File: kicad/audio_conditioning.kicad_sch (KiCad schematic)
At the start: 51 parts, among them Q5 MMUN2111LT1G, Q6 MMUN2111LT1G, Q7 MMBT3904, Q8 MMBT3904, U4 OPA1678, U5 OPA1678, U6 OPA1678

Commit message: started with PCB layout. Might want to move I2S
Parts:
- C24: renamed from C42; footprint (none) -> Capacitor_SMD:C_0805_2012Metric
- C25: renamed from C43; footprint (none) -> Capacitor_SMD:C_0805_2012Metric
- C26: renamed from C45; footprint (none) -> Capacitor_SMD:C_0402_1005Metric
- C27: renamed from C44; footprint (none) -> Capacitor_SMD:C_0402_1005Metric
- C28: renamed from C52; footprint (none) -> Capacitor_SMD:C_0603_1608Metric
- C29: renamed from C53; footprint (none) -> Capacitor_SMD:C_0603_1608Metric
- C30: renamed from C54; footprint (none) -> Capacitor_SMD:C_0603_1608Metric
- C31: renamed from C55; footprint (none) -> Capacitor_SMD:C_0603_1608Metric
- C32: renamed from C60; footprint (none) -> Capacitor_SMD:C_0402_1005Metric
- C33: renamed from C62; footprint (none) -> Capacitor_SMD:C_0603_1608Metric
- C34: renamed from C64; footprint (none) -> Capacitor_SMD:CP_Elec_4x5.4
- C35: renamed from C58; footprint (none) -> Capacitor_SMD:CP_Elec_4x5.4
- C36: renamed from C56; footprint (none) -> Capacitor_SMD:C_0603_1608Metric
- C37: renamed from C57; footprint (none) -> Capacitor_SMD:C_0603_1608Metric
- C38: renamed from C61; footprint (none) -> Capacitor_SMD:C_0402_1005Metric
- C39: renamed from C63; footprint (none) -> Capacitor_SMD:C_0603_1608Metric
- C40: renamed from C65; footprint (none) -> Capacitor_SMD:CP_Elec_4x5.4
- C41: renamed from C59; footprint (none) -> Capacitor_SMD:CP_Elec_4x5.4
- R20: renamed from R36; footprint (none) -> Resistor_SMD:R_0402_1005Metric
- R21: renamed from R37; footprint (none) -> Resistor_SMD:R_0402_1005Metric
- R22: renamed from R39; footprint (none) -> Resistor_SMD:R_0402_1005Metric
- R23: renamed from R40; footprint (none) -> Resistor_SMD:R_0402_1005Metric
- R24: renamed from R38; footprint (none) -> Resistor_SMD:R_0402_1005Metric
- R25: renamed from R41; footprint (none) -> Resistor_SMD:R_0402_1005Metric
- R26: renamed from R51; footprint (none) -> Resistor_SMD:R_0402_1005Metric
- R27: renamed from R57; footprint (none) -> Resistor_SMD:R_0402_1005Metric
- R28: renamed from R52; footprint (none) -> Resistor_SMD:R_0402_1005Metric
- R29: renamed from R58; footprint (none) -> Resistor_SMD:R_0402_1005Metric
- R30: renamed from R61; footprint (none) -> Resistor_SMD:R_0402_1005Metric
- R31: renamed from R55; footprint (none) -> Resistor_SMD:R_0402_1005Metric
- R32: renamed from R63; footprint (none) -> Resistor_SMD:R_0402_1005Metric
- R33: renamed from R65; footprint (none) -> Resistor_SMD:R_0402_1005Metric
- R34: renamed from R69; footprint (none) -> Resistor_SMD:R_0402_1005Metric
- R35: renamed from R67; footprint (none) -> Resistor_SMD:R_0402_1005Metric
- R36: renamed from R53; footprint (none) -> Resistor_SMD:R_0402_1005Metric
- R37: renamed from R59; footprint (none) -> Resistor_SMD:R_0402_1005Metric
- R38: renamed from R54; footprint (none) -> Resistor_SMD:R_0402_1005Metric
- R39: renamed from R60; footprint (none) -> Resistor_SMD:R_0402_1005Metric
- R40: renamed from R62; footprint (none) -> Resistor_SMD:R_0402_1005Metric
- R41: renamed from R56; footprint (none) -> Resistor_SMD:R_0402_1005Metric
- R42: renamed from R64; footprint (none) -> Resistor_SMD:R_0402_1005Metric
- R43: renamed from R66; footprint (none) -> Resistor_SMD:R_0402_1005Metric
- R44: renamed from R70; footprint (none) -> Resistor_SMD:R_0402_1005Metric
- R45: renamed from R68; footprint (none) -> Resistor_SMD:R_0402_1005Metric
- U4, U5, U6: footprint (none) -> Package_SO:SOIC-8_3.9x4.9mm_P1.27mm

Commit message: aaaa
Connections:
- net at C38.2, R37.2: now also U6.2 (-); no longer U6.6 (-)
- net at C40.1: now also U6.1; no longer U6.7
- net at C33.2, R29.2: now also U6.5 (+); no longer U6.3 (+)
- net at C32.2, R27.2: now also U6.6 (-); no longer U6.2 (-)
- net at C34.1: now also U6.7; no longer U6.1
- net at C39.2, R39.2: now also U6.3 (+); no longer U6.5 (+)
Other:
- moved on the sheet: U4C, U5C, U6C
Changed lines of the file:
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@@
 	)
 	(junction
-		(at 49.53 152.4)
+		(at 62.23 125.73)
 		(diameter 0)
 		(color 0 0 0 0)
@@
 	)
 	(junction
-		(at 45.72 176.53)
+		(at 58.42 149.86)
 		(diameter 0)
 		(color 0 0 0 0)
 	)
 	(junction
-		(at 45.72 152.4)
+		(at 58.42 125.73)
 		(diameter 0)
 		(color 0 0 0 0)
@@
 	)
 	(junction
-		(at 40.64 176.53)
+		(at 53.34 149.86)
 		(diameter 0)
 		(color 0 0 0 0)
@@
 	(wire
 		(pts
-			(xy 45.72 152.4) (xy 45.72 157.48)
+			(xy 58.42 125.73) (xy 58.42 130.81)
 		)
 		(stroke
@@
 	(wire
 		(pts
-			(xy 30.48 172.72) (xy 30.48 176.53)
+			(xy 43.18 146.05) (xy 43.18 149.86)
 		)
 		(stroke
@@
 	(wire
 		(pts
-			(xy 45.72 172.72) (xy 45.72 176.53)
+			(xy 58.42 146.05) (xy 58.42 149.86)
 		)
 		(stroke
@@
 	(wire
 		(pts
-			(xy 62.23 157.48) (xy 62.23 152.4)
+			(xy 74.93 130.81) (xy 74.93 125.73)
 		)
 		(stroke
@@
 	(wire
 		(pts
-			(xy 30.48 157.48) (xy 30.48 152.4)
+			(xy 43.18 130.81) (xy 43.18 125.73)
 		)
 		(stroke
@@
 	(wire
 		(pts
-			(xy 30.48 176.53) (xy 40.64 176.53)
+			(xy 43.18 149.86) (xy 53.34 149.86)
 		)
 		(stroke
@@
 	(wire
 		(pts
-			(xy 62.23 172.72) (xy 62.23 176.53)
+			(xy 74.93 146.05) (xy 74.93 149.86)
 		)
 		(stroke
@@
 	(wire
 		(pts
-			(xy 49.53 152.4) (xy 45.72 152.4)
+			(xy 62.23 125.73) (xy 58.42 125.73)
 		)
 		(stroke
@@
 	(wire
 		(pts
-			(xy 40.64 176.53) (xy 45.72 176.53)
+			(xy 53.34 149.86) (xy 58.42 149.86)
 		)
 		(stroke
@@
 	(wire
 		(pts
-			(xy 40.64 176.53) (xy 40.64 179.07)
+			(xy 53.34 149.86) (xy 53.34 152.4)
 		)
 		(stroke
@@
 	(wire
 		(pts
-			(xy 62.23 152.4) (xy 49.53 152.4)
+			(xy 74.93 125.73) (xy 62.23 125.73)
 		)
 		(stroke
@@
 	(wire
 		(pts
-			(xy 30.48 152.4) (xy 45.72 152.4)
+			(xy 43.18 125.73) (xy 58.42 125.73)
 		)
 		(stroke
@@
 	(wire
 		(pts
-			(xy 62.23 176.53) (xy 45.72 176.53)
+			(xy 74.93 149.86) (xy 58.42 149.86)
 		)
 		(stroke
@@
 	(symbol
 		(lib_id "Amplifier_Operational:OPA1678")
-		(at 33.02 165.1 0)
+		(at 45.72 138.43 0)
 		(unit 3)
 		(body_style 1)
@@
 		(dnp no)
 		(property "Reference" "U4"
-			(at 32.512 167.386 0)
+			(at 45.212 140.716 0)
 			(show_name no)
 			(do_not_autoplace no)
@@
 		)
 		(property "Value" "OPA1678"
-			(at 32.258 164.592 0)
+			(at 44.958 137.922 0)
 			(show_name no)
 			(do_not_autoplace no)
@@
 		)
 		(property "Footprint" "Package_SO:SOIC-8_3.9x4.9mm_P1.27mm"
-			(at 33.02 165.1 0)
+			(at 45.72 138.43 0)
 			(hide yes)
 			(show_name no)
@@
 		)
 		(property "Datasheet" "http://www.ti.com/lit/ds/symlink/opa1678.pdf"
-			(at 33.02 165.1 0)
+			(at 45.72 138.43 0)
 			(hide yes)
 			(show_name no)
@@
 		)
 		(property "Description" "Low-Distortion Audio Operational Amplifiers, SOIC-8/VSSOP-8"
-			(at 33.02 165.1 0)
+			(at 45.72 138.43 0)
 			(hide yes)
 			(show_name no)
@@
 		(at 182.88 107.95 0)
 		(mirror x)
-		(unit 2)
+		(unit 1)
 		(body_style 1)
 		(exclude_from_sim no)
@@
 				(path "/820f84be-8ed9-43fe-8cf8-9ca6f73c98d0"
 					(reference "U6")
-					(unit 2)
+					(unit 1)
 				)
 			)
@@
 	(symbol
 		(lib_id "Amplifier_Operational:OPA1678")
-		(at 43.18 165.1 0)
+		(at 55.88 138.43 0)
 		(mirror y)
 		(unit 3)
@@
 		(dnp no)
 		(property "Reference" "U5"
-			(at 46.99 166.3701 0)
+			(at 59.69 139.7001 0)
 			(show_name no)
 			(do_not_autoplace no)
@@
 		)
 		(property "Value" "OPA1678"
-			(at 46.99 163.8301 0)
+			(at 59.69 137.1601 0)
 			(show_name no)
 			(do_not_autoplace no)
@@
 		)
 		(property "Footprint" "Package_SO:SOIC-8_3.9x4.9mm_P1.27mm"
-			(at 43.18 165.1 0)
+			(at 55.88 138.43 0)
 			(hide yes)
 			(show_name no)
@@
 		)
 		(property "Datasheet" "http://www.ti.com/lit/ds/symlink/opa1678.pdf"
-			(at 43.18 165.1 0)
+			(at 55.88 138.43 0)
 			(hide yes)
 			(show_name no)
@@
 		)
 		(property "Description" "Low-Distortion Audio Operational Amplifiers, SOIC-8/VSSOP-8"
-			(at 43.18 165.1 0)
+			(at 55.88 138.43 0)
 			(hide yes)
 			(show_name no)
@@
 		(at 182.88 44.45 0)
 		(mirror x)
-		(unit 1)
+		(unit 2)
 		(body_style 1)
 		(exclude_from_sim no)
@@
 				(path "/820f84be-8ed9-43fe-8cf8-9ca6f73c98d0"
 					(reference "U6")
-					(unit 1)
+					(unit 2)
 				)
 			)
@@
 	(symbol
 		(lib_id "power:GND")
-		(at 40.64 179.07 0)
+		(at 53.34 152.4 0)
 		(unit 1)
 		(body_style 1)
@@
 		(fields_autoplaced yes)
 		(property "Reference" "#PWR052"
-			(at 40.64 185.42 0)
+			(at 53.34 158.75 0)
 			(hide yes)
 			(show_name no)
@@
 		)
 		(property "Value" "GND"
-			(at 40.64 184.15 0)
+			(at 53.34 157.48 0)
 			(hide yes)
 			(show_name no)
@@
 		)
 		(property "Footprint" ""
-			(at 40.64 179.07 0)
+			(at 53.34 152.4 0)
 			(hide yes)
 			(show_name no)
@@
 		)
 		(property "Datasheet" ""
-			(at 40.64 179.07 0)
+			(at 53.34 152.4 0)
 			(hide yes)
 			(show_name no)
@@
 		)
 		(property "Description" "Power symbol creates a global label with name \"GND\" , ground"
-			(at 40.64 179.07 0)
+			(at 53.34 152.4 0)
 			(hide yes)
 			(show_name no)
@@
 	(symbol
 		(lib_id "Amplifier_Operational:OPA1678")
-		(at 59.69 165.1 0)
+		(at 72.39 138.43 0)
 		(mirror y)
 		(unit 3)
@@
 		(dnp no)
 		(property "Reference" "U6"
-			(at 64.77 166.116 0)
+			(at 77.47 139.446 0)
 			(show_name no)
 			(do_not_autoplace no)
@@
 		)
 		(property "Value" "OPA1678"
-			(at 64.77 163.83 0)
+			(at 77.47 137.16 0)
 			(show_name no)
 			(do_not_autoplace no)
@@
 		)
 		(property "Footprint" "Package_SO:SOIC-8_3.9x4.9mm_P1.27mm"
-			(at 59.69 165.1 0)
+			(at 72.39 138.43 0)
 			(hide yes)
 			(show_name no)
@@
 		)
 		(property "Datasheet" "http://www.ti.com/lit/ds/symlink/opa1678.pdf"
-			(at 59.69 165.1 0)
+			(at 72.39 138.43 0)
 			(hide yes)
 			(show_name no)
@@
 		)
 		(property "Description" "Low-Distortion Audio Operational Amplifiers, SOIC-8/VSSOP-8"
-			(at 59.69 165.1 0)
+			(at 72.39 138.43 0)
 			(hide yes)
 			(show_name no)
@@
 	(symbol
 		(lib_id "power:+5VA")
-		(at 49.53 152.4 0)
+		(at 62.23 125.73 0)
 		(unit 1)
 		(body_style 1)
@@
 		(fields_autoplaced yes)
 		(property "Reference" "#PWR053"
-			(at 49.53 156.21 0)
+			(at 62.23 129.54 0)
 			(hide yes)
 			(show_name no)
@@
 		)
 		(property "Value" "+5VA"
-			(at 49.53 147.32 0)
+			(at 62.23 120.65 0)
 			(show_name no)
 			(do_not_autoplace no)
@@
 		)
 		(property "Footprint" ""
-			(at 49.53 152.4 0)
+			(at 62.23 125.73 0)
 			(hide yes)
 			(show_name no)
@@
 		)
 		(property "Datasheet" ""
-			(at 49.53 152.4 0)
+			(at 62.23 125.73 0)
 			(hide yes)
 			(show_name no)
@@
 		)
 		(property "Description" "Power symbol creates a global label with name \"+5VA\""
-			(at 49.53 152.4 0)
+			(at 62.23 125.73 0)
 			(hide yes)
 			(show_name no)

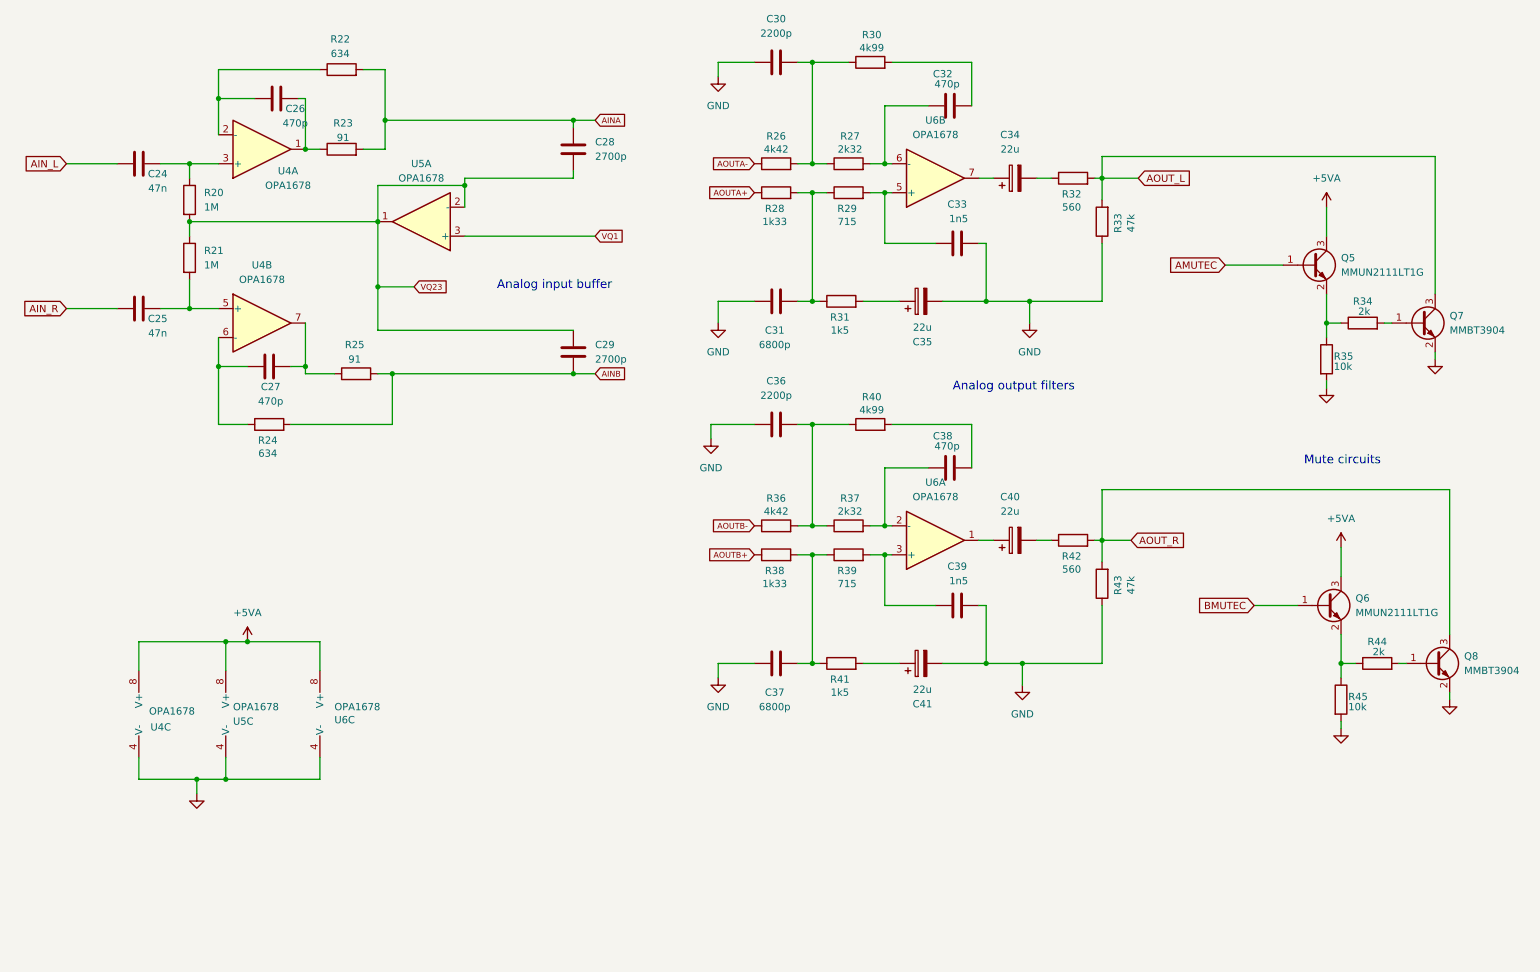
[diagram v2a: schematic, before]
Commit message: moved to hierarchical sheets
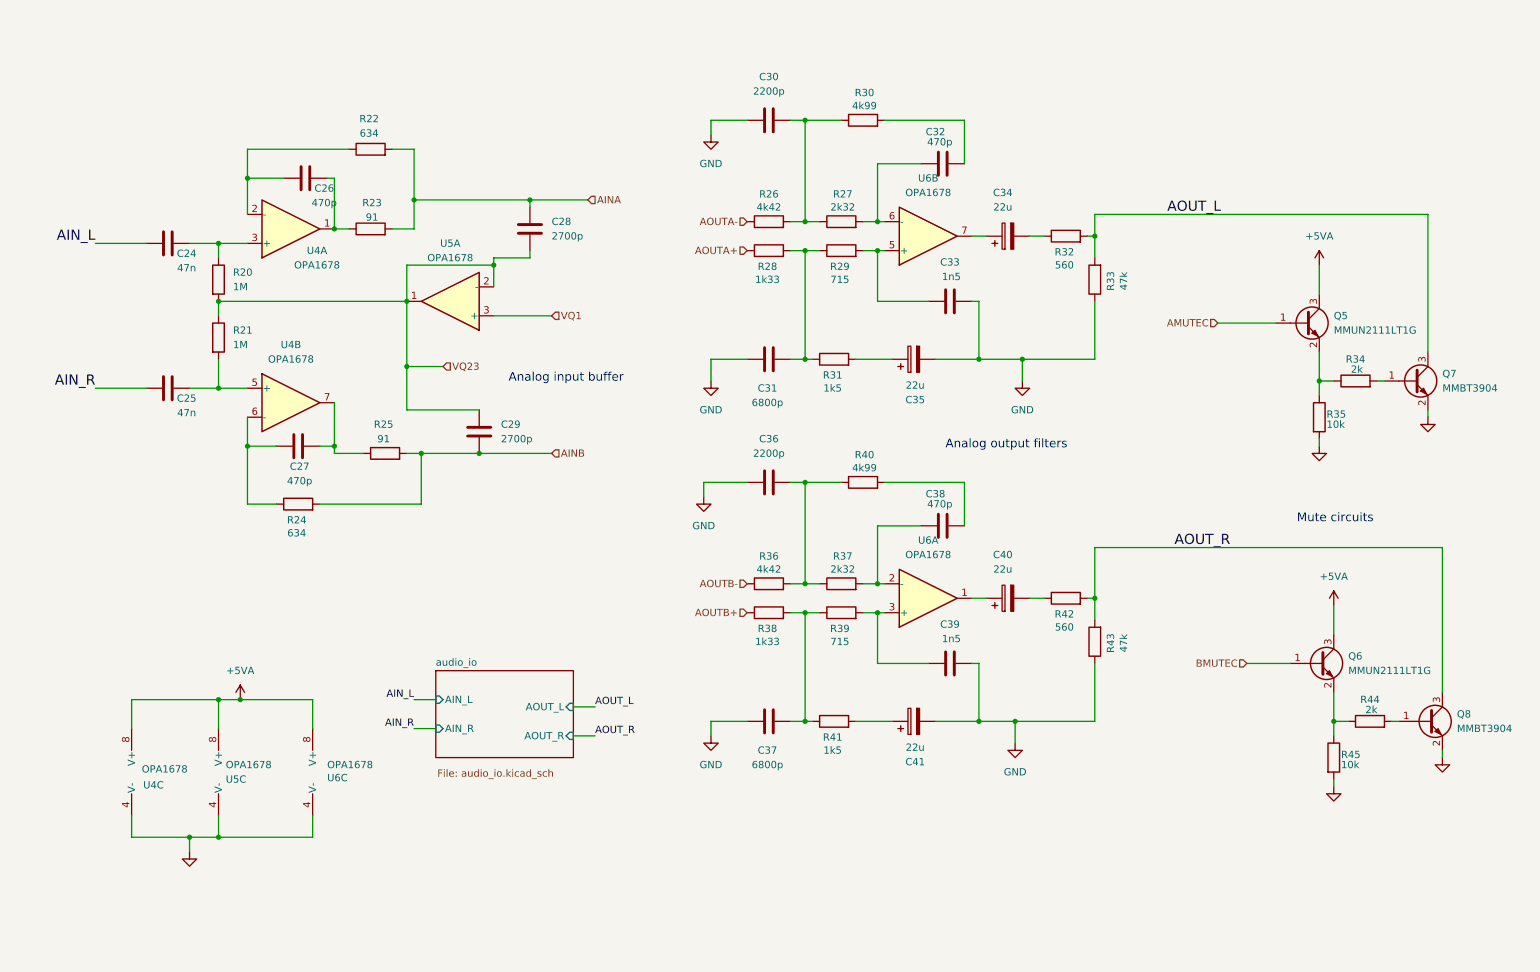
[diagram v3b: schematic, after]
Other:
- added sheet audio_io (audio_io.kicad_sch)
